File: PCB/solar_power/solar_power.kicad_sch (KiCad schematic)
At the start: 16 parts, among them U1 BQ25570

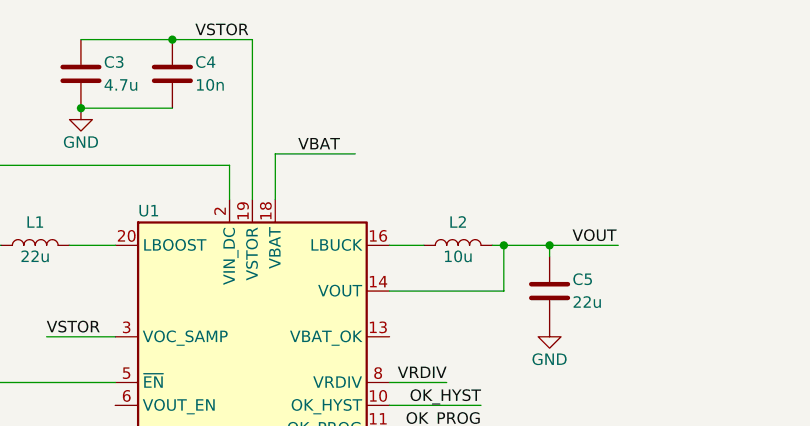
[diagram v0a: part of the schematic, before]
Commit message: Added 18650 battery holder to library and solar PCB
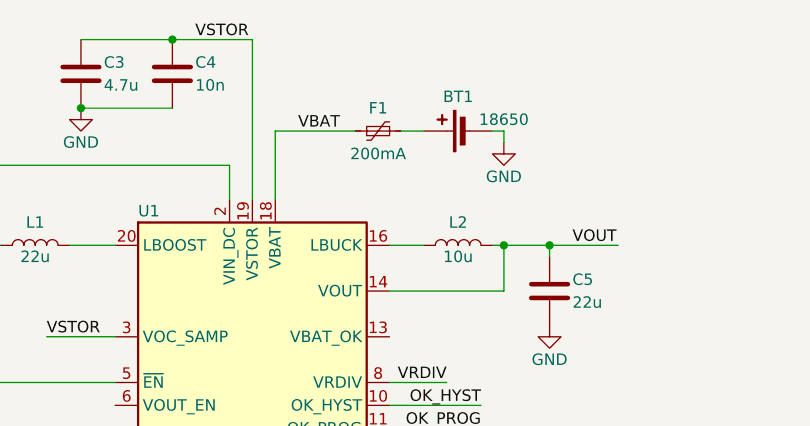
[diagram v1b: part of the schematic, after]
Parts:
- added BT1: 18650, DWlib:Keystone_1043P_1x18650, symbol Device:Battery_Cell
- added F1: 200mA, Fuse:Fuse_1206_3216Metric, symbol Device:Polyfuse_Small
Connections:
- net GND: now also BT1.2 (-)
- net VBAT: now also F1.1
- new net: BT1.1 (+), F1.2

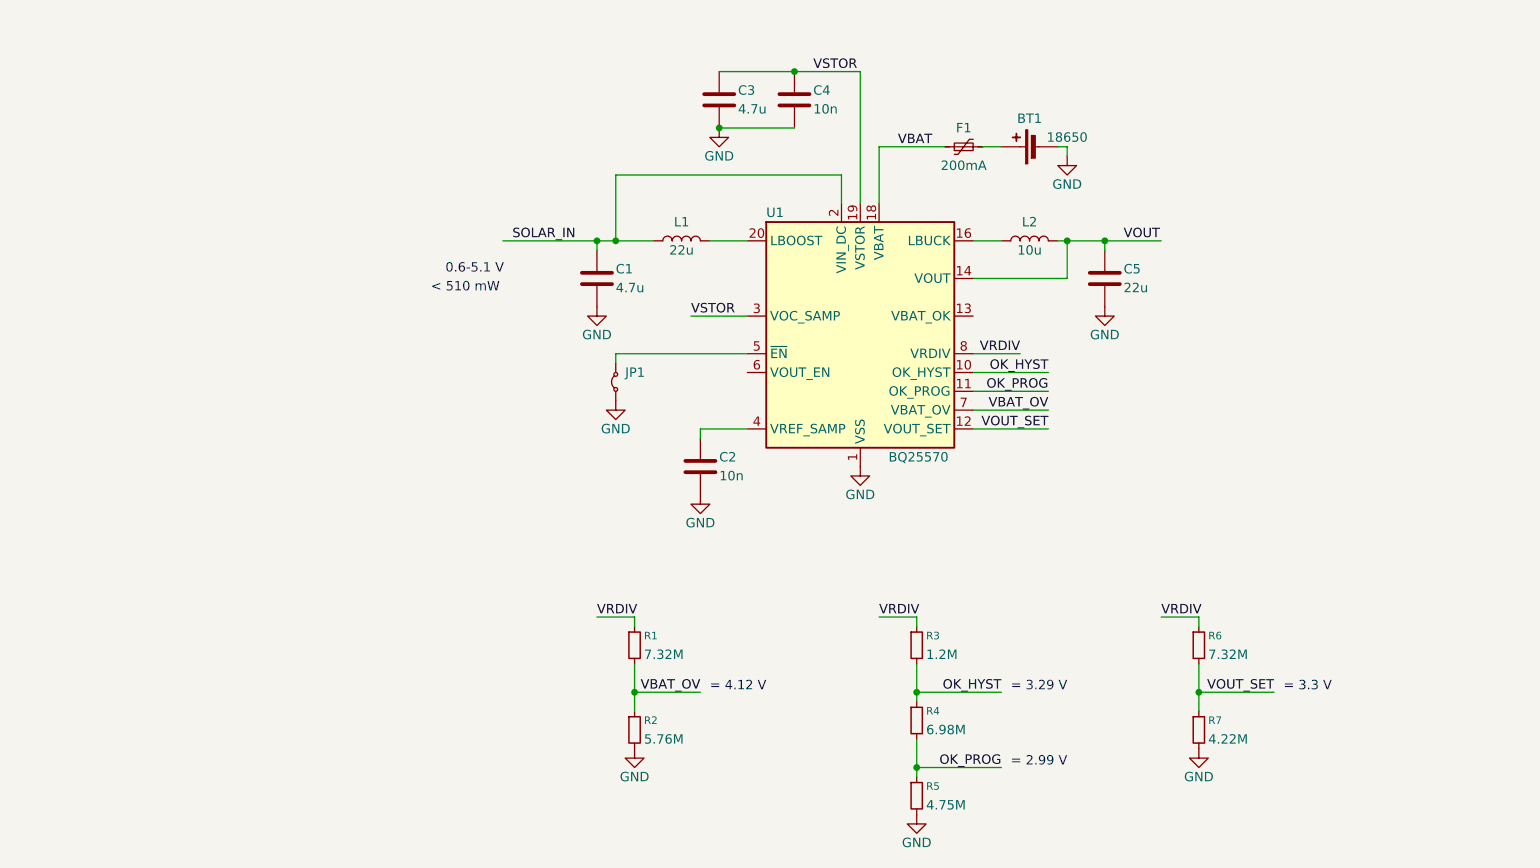
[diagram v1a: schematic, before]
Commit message: Added filtering and connectors to solar PCB with 3D models
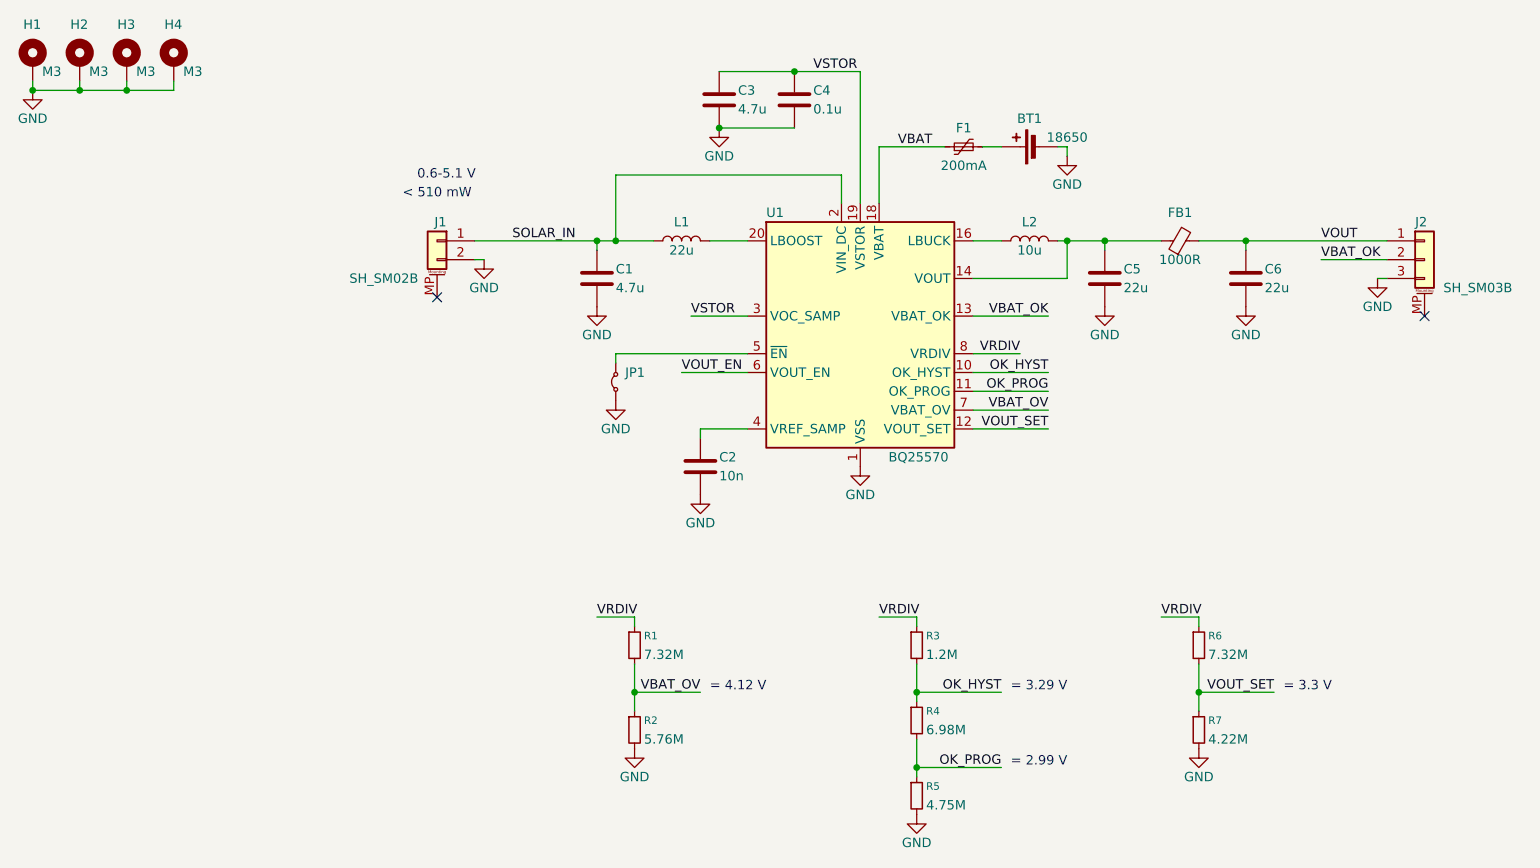
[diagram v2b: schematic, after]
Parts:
- added C6: 22u, Capacitor_SMD:C_0805_2012Metric, symbol Device:C
- added FB1: 1000R, Inductor_SMD:L_0603_1608Metric, symbol Device:FerriteBead_Small
- added H1, H2, H3, H4: M3, MountingHole:MountingHole_3.2mm_M3_Pad, symbol Mechanical:MountingHole_Pad
- added J1: SH_SM02B, Connector_JST:JST_SH_SM02B-SRSS-TB_1x02-1MP_P1.00mm_Horizontal, symbol Connector_Generic_MountingPin:Conn_01x02_MountingPin
- added J2: SH_SM03B, Connector_JST:JST_SH_SM03B-SRSS-TB_1x03-1MP_P1.00mm_Horizontal, symbol Connector_Generic_MountingPin:Conn_01x03_MountingPin
- C4: value 10n -> 0.1u
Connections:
- net GND: now also C6.2, H1.1, H2.1, H3.1, H4.1, J1.2 (Pin_2), J2.3 (Pin_3)
- net SOLAR_IN: now also J1.1 (Pin_1)
- net VOUT: now also C6.1, FB1.2, J2.1 (Pin_1); no longer C5.1, L2.2, U1.14 (VOUT)
- net VBAT_OK: now reaches U1.13 (VBAT_OK)
- net VBAT_OK: now also J2.2 (Pin_2)
- net VOUT_EN: now reaches U1.6 (VOUT_EN)
- new net: C5.1, FB1.1, L2.2, U1.14 (VOUT)
- no-connect marks 0 -> 2
